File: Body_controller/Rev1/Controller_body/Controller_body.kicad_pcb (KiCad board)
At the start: 2 copper layers, 40.6 x 91.2 mm, 23 parts, among them J1 Conn_01x06_Socket, J2 Conn_01x03_Socket, U1 PCF8575PWR

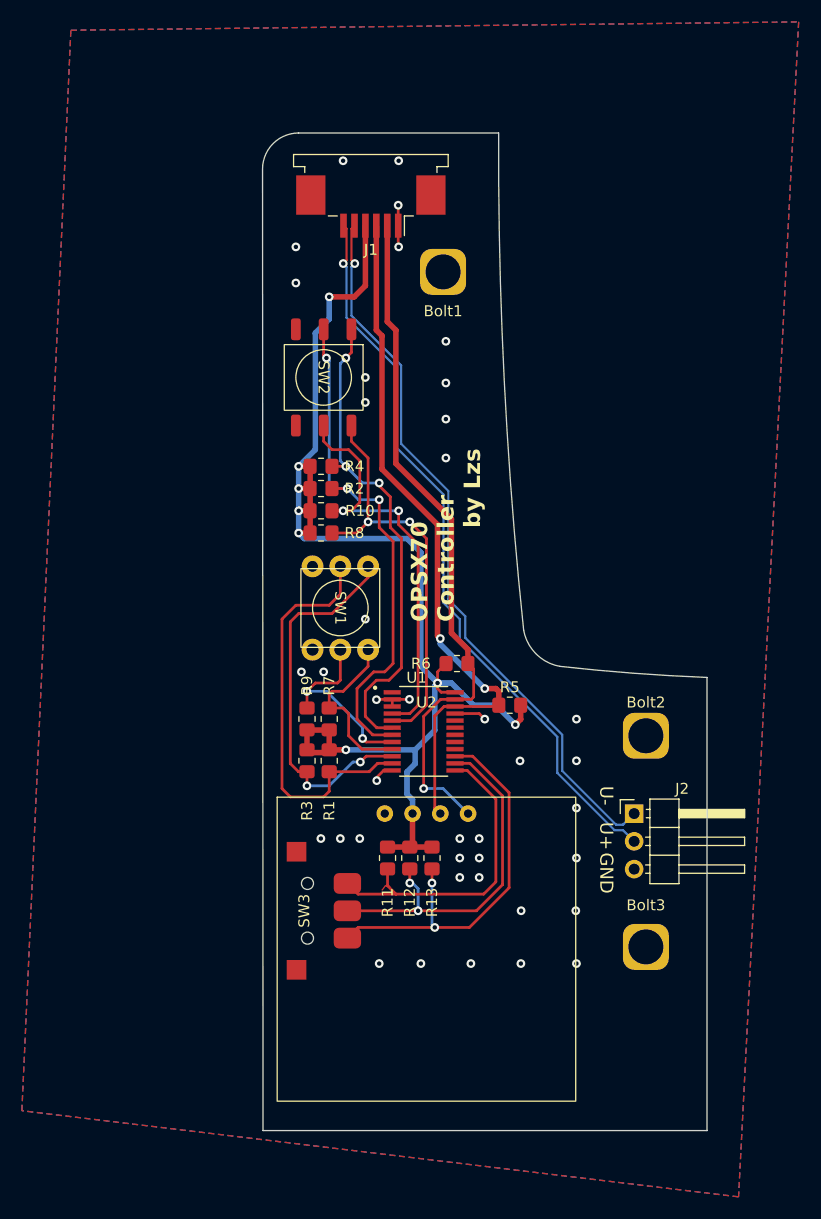
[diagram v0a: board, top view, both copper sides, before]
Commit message: update to Kicad 8.0 & update BodyController to Rev 2.0
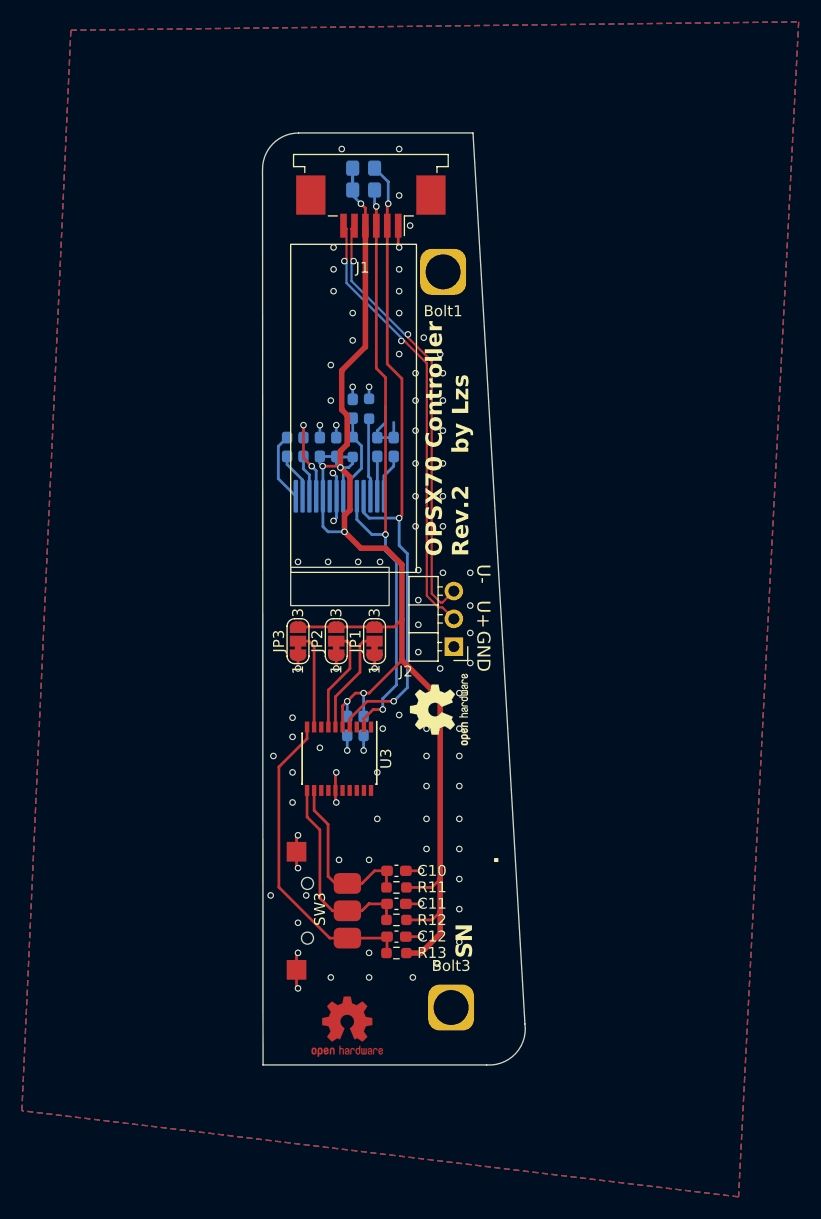
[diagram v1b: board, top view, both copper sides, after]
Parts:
- removed Bolt2: ~, 0JIMMY:M3_Bolt
- removed R10, R3, R4, R7, R8, R9: 100k, Resistor_SMD:R_0805_2012Metric_Pad1.20x1.40mm_HandSolder
- removed SW1: ~, SW_CODED:GSMR_16
- removed SW2: ~, SW_CODED:GSMR_10S
- removed U1: PCF8575PWR, PCF8575PWR:SOP65P640X120-24N
- removed U2: ~, 0JIMMY:OLED 0.96 i2c
- added C1: 1uF, Capacitor_SMD:C_0603_1608Metric_Pad1.08x0.95mm_HandSolder, B.Cu at (82.0, 78.5)
- added C10: 1uF, Capacitor_SMD:C_0603_1608Metric_Pad1.08x0.95mm_HandSolder, F.Cu at (92.0, 117.2)
- added C11: 1uF, Capacitor_SMD:C_0603_1608Metric_Pad1.08x0.95mm_HandSolder, F.Cu at (92.0, 120.3)
- added C12: 1uF, Capacitor_SMD:C_0603_1608Metric_Pad1.08x0.95mm_HandSolder, F.Cu at (92.0, 123.3)
- added C2: 1uF, Capacitor_SMD:C_0603_1608Metric_Pad1.08x0.95mm_HandSolder, B.Cu at (83.5, 78.5)
- added C3: 2.2uF, Capacitor_SMD:C_0603_1608Metric_Pad1.08x0.95mm_HandSolder, B.Cu at (91.8, 78.5)
- added C4: 4.7uF, Capacitor_SMD:C_0603_1608Metric_Pad1.08x0.95mm_HandSolder, B.Cu at (90.2, 78.5)
- added C5: 1uF, Capacitor_SMD:C_0603_1608Metric_Pad1.08x0.95mm_HandSolder, B.Cu at (86.5, 78.5)
- added C6: 1uF, Capacitor_SMD:C_0603_1608Metric_Pad1.08x0.95mm_HandSolder, B.Cu at (85.0, 78.5)
- added C7: 1uF(4.7uF), Capacitor_SMD:C_0603_1608Metric_Pad1.08x0.95mm_HandSolder, B.Cu at (88.0, 75.0)
- added C8: 2.2uF, Capacitor_SMD:C_0603_1608Metric_Pad1.08x0.95mm_HandSolder, B.Cu at (87.5, 104.0)
- added C9: 1uF, Capacitor_SMD:C_0603_1608Metric_Pad1.08x0.95mm_HandSolder, B.Cu at (89.0, 104.0)
- added Disp1: ~, KiCadLib:SSD1306_0.91_i2c, B.Cu at (86.8, 92.5)
- added JP1: SolderJumper_3_Bridged12, Jumper:SolderJumper-3_P1.3mm_Bridged12_RoundedPad1.0x1.5mm_NumberLabels, F.Cu at (90.0, 96.2)
- added JP2: SolderJumper_3_Bridged12, Jumper:SolderJumper-3_P1.3mm_Bridged12_RoundedPad1.0x1.5mm_NumberLabels, F.Cu at (86.5, 96.2)
- added JP3: SolderJumper_3_Bridged12, Jumper:SolderJumper-3_P1.3mm_Bridged12_RoundedPad1.0x1.5mm_NumberLabels, F.Cu at (83.0, 96.2)
- added REF**: OSHW-Logo2_7.3x6mm_SilkScreen, Symbol:OSHW-Logo2_7.3x6mm_SilkScreen, F.Cu at (96.0, 102.5)
- added REF**: OSHW-Logo2_7.3x6mm_Copper, Symbol:OSHW-Logo2_7.3x6mm_Copper, F.Cu at (87.5, 131.5)
- added U3: PCF8574ATS, Package_SO:SSOP-20_4.4x6.5mm_P0.65mm, F.Cu at (86.8, 107.0)
- R1: value 100k -> 390k; footprint Resistor_SMD:R_0805_2012Metric_Pad1.20x1.40mm_HandSolder -> Resistor_SMD:R_0603_1608Metric_Pad0.98x0.95mm_HandSolder; moved to B.Cu
- R11, R12, R13: footprint Resistor_SMD:R_0805_2012Metric_Pad1.20x1.40mm_HandSolder -> Resistor_SMD:R_0603_1608Metric_Pad0.98x0.95mm_HandSolder
- R2: value 100k -> 4.7k; footprint Resistor_SMD:R_0805_2012Metric_Pad1.20x1.40mm_HandSolder -> Resistor_SMD:R_0603_1608Metric_Pad0.98x0.95mm_HandSolder; moved to B.Cu
- R5, R6: moved to B.Cu
- moved R5 49.0 mm to (89.0, 55.0), turned to 180 degrees
- moved R6 46.1 mm to (89.0, 53.0)
- moved R1 32.4 mm to (89.5, 75.0)
- moved J2 22.5 mm to (97.2, 96.8), turned to 180 degrees
- moved Bolt3 18.7 mm to (97.0, 129.8)
- moved R13 9.28 mm to (92.0, 124.8), turned to 0 degrees
- moved R12 5.79 mm to (92.0, 121.7), turned to 0 degrees
- moved R2 4.77 mm to (88.0, 78.5), turned to 90 degrees
- moved R11 2.81 mm to (92.0, 118.8), turned to 0 degrees
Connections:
- J2 pad 1: /UD- -> GND
- J2 pad 3: GND -> /UD-
- R1 pad 1: /M_8 -> Net-(Disp1-IREF)
- R1 pad 2: +3.3V -> GND
- R2 pad 1: /A_8 -> +3.3V
- R2 pad 2: +3.3V -> Net-(Disp1-RES#)
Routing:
- net /A_8: track 47.2 -> 0.00 mm, vias 3 -> 0
- net /A_4: track 45.2 -> 0.00 mm, vias 3 -> 0
- net /A_1: track 38.4 -> 0.00 mm, vias 2 -> 0
- net /A_2: track 38.1 -> 0.00 mm, vias 2 -> 0
- net /M_8: track 37.0 -> 0.00 mm
- net /M_4: track 34.8 -> 0.00 mm, vias 2 -> 0
- net /UD+: track 68.0 -> 40.7 mm, vias 1 -> 2
- net /UD-: track 67.2 -> 39.9 mm, vias 1 -> 2
- net GND: track 12.4 -> 37.1 mm, vias 40 -> 99
- net /M_1: track 18.1 -> 0.00 mm, vias 2 -> 0
- net +3.3V: track 118.4 -> 135.3 mm, vias 8 -> 6
- net /M_2: track 15.9 -> 0.00 mm
- net /SW_PUSH: track 33.2 -> 18.7 mm, vias 2 -> 0
- net /SW_B: track 29.4 -> 16.1 mm
- net Net-(JP1-C): track 0.00 -> 9.92 mm
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- removed copper zone on F.Cu, net /SW_B
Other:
- board size 40.6 x 91.2 mm -> 24 x 85.2 mm
- board text added: "OPSX70 Controller Rev.2 by Lzs"
- board text added: "SN ."
- board text removed: "OPSX70 Controller by Lzs"
